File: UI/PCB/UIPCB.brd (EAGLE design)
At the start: 31.7 x 53 mm, 9 parts

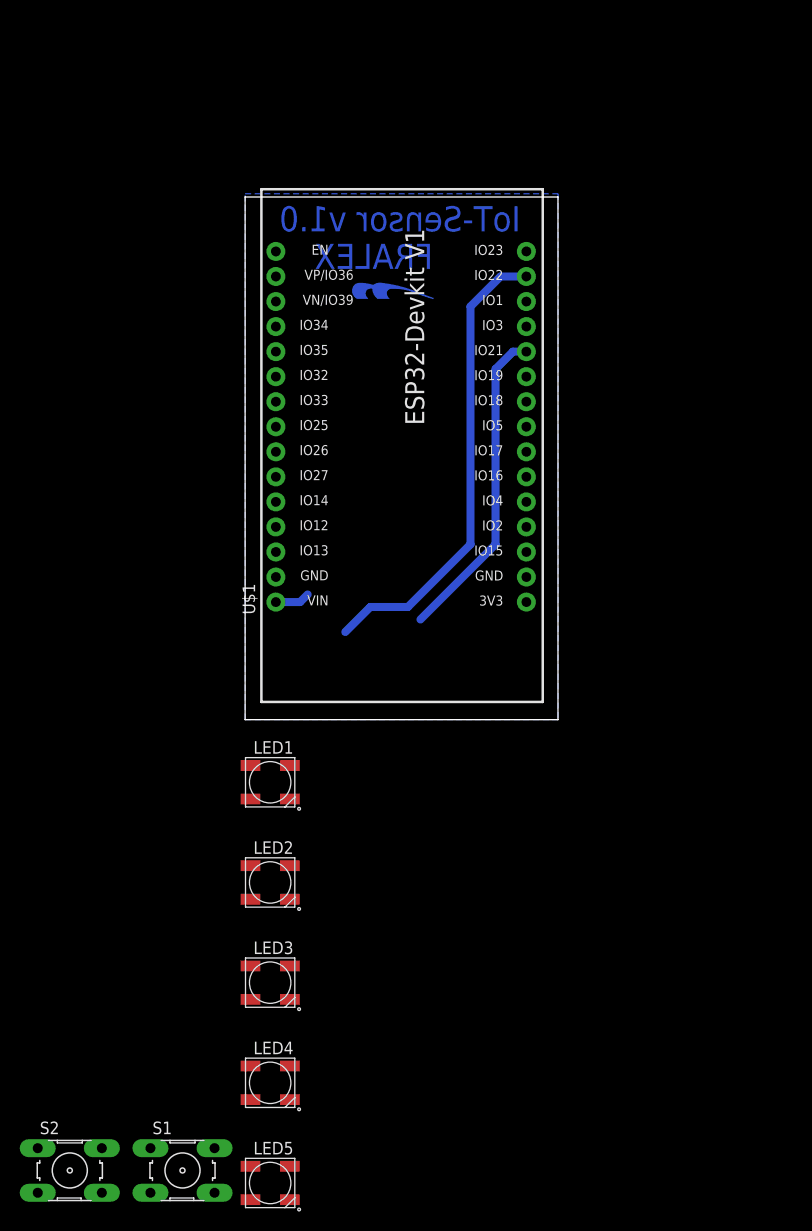
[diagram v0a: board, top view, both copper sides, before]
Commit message: added ui board added dashborad basic
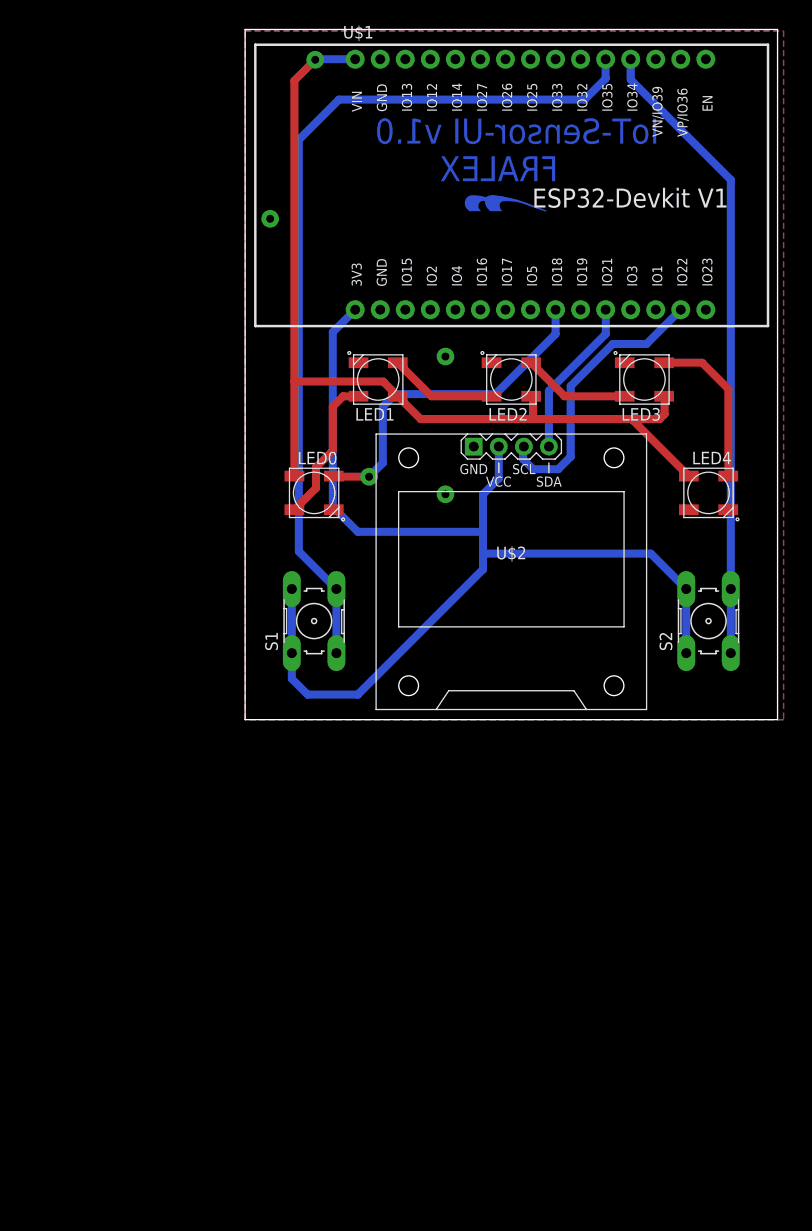
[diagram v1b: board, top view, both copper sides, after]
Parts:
- removed LED5: WS2812B, WS2812B:WS2812B
- added LED0: WS2812B, WS2812B:WS2812B
- added U$2: DISPLAY-OLED-128X64-I2C, SSD1306:DISPLAY-OLED-128X64-I2C
- moved S2 85.4 mm to (47.0, 10.0), turned to 90 degrees
- moved LED4 74.5 mm to (47.0, 23.0)
- moved LED3 72.0 mm to (40.5, 34.5), turned to 180 degrees
- moved S1 57.3 mm to (7.00, 10.0), turned to 90 degrees
- moved LED2 56.6 mm to (27.0, 34.5), turned to 180 degrees
- moved LED1 42.3 mm to (13.5, 34.5), turned to 180 degrees
- moved U$1 27.9 mm to (27.7, 53.8), turned to 0 degrees
- moved U$4 14.5 mm to (21.6, 50.8)
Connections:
- removed net N$4 (its old number): LED1.DIN, LED5.DOUT
- removed net N$5: LED1.VSS, LED2.VSS, LED3.VSS, LED4.VSS, LED5.VSS, U$1.GND@1
- removed net N$6: LED3.DIN, U$1.D18
- new net 3V3: S1.1, S1.2, S2.1, S2.2, U$1.3V3, U$2.2
- new net GND: LED0.VSS, LED1.VSS, LED2.VSS, LED3.VSS, LED4.VSS, U$1.GND@1, U$2.1
- new net LEDDATA: LED0.DIN, U$1.D18
- new net N$1: LED0.DOUT, LED1.DIN
- new net SW1: S1.3, S1.4, U$1.D35
- new net SW2: S2.3, S2.4, U$1.D34
- net 5V: now also LED0.VDD; no longer LED5.VDD
- net N$2: now also LED1.DOUT; no longer LED4.DOUT
- net N$3: now also LED3.DIN; no longer LED5.DIN
- net SCL: now also U$2.3
- net SDA: now also U$2.4
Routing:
- net 3V3: track 0.00 -> 113.4 mm
- net 5V: track 3.55 -> 98.9 mm, vias 0 -> 1
- net SW1: track 0.00 -> 89.3 mm
- net SW2: track 0.00 -> 64.4 mm
- net LEDDATA: track 0.00 -> 34.3 mm, vias 0 -> 1
- net SCL: track 47.4 -> 28.6 mm
- net N$4: track 0.00 -> 16.4 mm
- net SDA: track 32.4 -> 16.3 mm
- net N$1: track 0.00 -> 15.1 mm
- net N$3: track 0.00 -> 10.9 mm
- net N$2: track 0.00 -> 10.9 mm
- added copper zone on layer 1, net GND
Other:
- board size 31.7 x 53 mm -> 54 x 70 mm
- board text added: "IoT-Sensor-UI v1.0"
- board text removed: "IoT-Sensor v1.0"
